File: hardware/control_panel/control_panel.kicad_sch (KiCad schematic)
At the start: 15 parts, among them J1 display, J13 motion and brightness sensors, J2 Conn_02x02_Odd_Even, J3 40HAT, J6 Conn_01x02, U3 TXB0108DQSR, U8 BCT0102

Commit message: hw layout
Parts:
- J3: footprint Connector_PinSocket_2.54mm:PinSocket_2x20_P2.54mm_Vertical -> project_footprints:raspberry_pi
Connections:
- net MOT: now also J13.2 (Pin_2), J3.7 (BCM4); no longer J13.4 (Pin_4)
- net RF.CE: now also U3.8 (A6); no longer U3.7 (A5)
- net RF.IRQ: now also U3.7 (A5); no longer U3.8 (A6)
- net SCL: now also J13.3 (Pin_3); no longer J13.2 (Pin_2)
- net SDA: now also J13.4 (Pin_4); no longer J13.3 (Pin_3)
- net UC.CE: now also U3.13 (B6); no longer U3.14 (B5)
- net UC.IRQ: now also U3.14 (B5); no longer U3.13 (B6)
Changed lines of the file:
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@@
     (stroke (width 0) (type default))
   )
-  (bus_entry (at 77.47 204.47) (size -2.54 2.54)
+  (bus_entry (at 77.47 201.93) (size -2.54 2.54)
     (stroke (width 0) (type default))
   )
@@
     (stroke (width 0) (type default))
   )
-  (bus_entry (at 77.47 201.93) (size -2.54 2.54)
+  (bus_entry (at 77.47 199.39) (size -2.54 2.54)
     (stroke (width 0) (type default))
   )
@@
     (stroke (width 0) (type default))
   )
-  (wire (pts (xy 74.93 204.47) (xy 68.58 204.47))
+  (wire (pts (xy 74.93 201.93) (xy 68.58 201.93))
     (stroke (width 0) (type default))
   )
@@
     (stroke (width 0) (type default))
   )
-  (bus (pts (xy 80.01 201.93) (xy 77.47 201.93))
+  (bus (pts (xy 80.01 199.39) (xy 77.47 199.39))
     (stroke (width 0) (type default))
   )
@@
     (stroke (width 0) (type default))
   )
-  (wire (pts (xy 68.58 201.93) (xy 71.12 201.93))
+  (wire (pts (xy 68.58 207.01) (xy 71.12 207.01))
     (stroke (width 0) (type default))
   )
@@
     (stroke (width 0) (type solid))
   )
-  (wire (pts (xy 74.93 207.01) (xy 68.58 207.01))
+  (wire (pts (xy 74.93 204.47) (xy 68.58 204.47))
     (stroke (width 0) (type default))
   )
@@
     (stroke (width 0) (type default))
   )
+  (wire (pts (xy 44.45 64.77) (xy 50.8 64.77))
+    (stroke (width 0) (type default))
+  )
   (wire (pts (xy 43.18 74.93) (xy 50.8 74.93))
     (stroke (width 0) (type default))
@@
     (stroke (width 0) (type default))
   )
-  (bus (pts (xy 77.47 201.93) (xy 77.47 204.47))
+  (bus (pts (xy 77.47 199.39) (xy 77.47 201.93))
     (stroke (width 0) (type default))
   )
@@
     (effects (font (size 1.27 1.27)) (justify right bottom))
   )
-  (label "RF.CE" (at 137.16 121.92 180) (fields_autoplaced)
+  (label "RF.CE" (at 137.16 124.46 180) (fields_autoplaced)
     (effects (font (size 1.27 1.27)) (justify right bottom))
   )
@@
     (effects (font (size 1.27 1.27)) (justify left bottom))
   )
-  (label "UC.IRQ" (at 157.48 124.46 0) (fields_autoplaced)
+  (label "UC.IRQ" (at 157.48 121.92 0) (fields_autoplaced)
     (effects (font (size 1.27 1.27)) (justify left bottom))
   )
@@
     (effects (font (size 1.27 1.27)) (justify left bottom))
   )
-  (label "MOT" (at 71.12 201.93 0) (fields_autoplaced)
+  (label "MOT" (at 71.12 207.01 0) (fields_autoplaced)
     (effects (font (size 1.27 1.27)) (justify left bottom))
   )
@@
     (effects (font (size 1.27 1.27)) (justify right bottom))
   )
-  (label "SDA" (at 71.12 204.47 0) (fields_autoplaced)
+  (label "SDA" (at 71.12 201.93 0) (fields_autoplaced)
     (effects (font (size 1.27 1.27)) (justify left bottom))
   )
@@
     (effects (font (size 1.27 1.27)) (justify left bottom))
   )
-  (label "SCL" (at 71.12 207.01 0) (fields_autoplaced)
+  (label "SCL" (at 71.12 204.47 0) (fields_autoplaced)
     (effects (font (size 1.27 1.27)) (justify left bottom))
   )
@@
     (effects (font (size 1.27 1.27)) (justify left bottom))
   )
-  (label "UC.CE" (at 157.48 121.92 0) (fields_autoplaced)
-    (effects (font (size 1.27 1.27)) (justify left bottom))
-  )
-  (label "RF.IRQ" (at 137.16 124.46 180) (fields_autoplaced)
+  (label "UC.CE" (at 157.48 124.46 0) (fields_autoplaced)
+    (effects (font (size 1.27 1.27)) (justify left bottom))
+  )
+  (label "RF.IRQ" (at 137.16 121.92 180) (fields_autoplaced)
     (effects (font (size 1.27 1.27)) (justify right bottom))
   )
@@
     (effects (font (size 1.27 1.27)) (justify right bottom))
   )
-  (label "{I2C}" (at 80.01 201.93 0) (fields_autoplaced)
+  (label "{I2C}" (at 80.01 199.39 0) (fields_autoplaced)
     (effects (font (size 1.27 1.27)) (justify left bottom))
   )
@@
     (effects (font (size 1.27 1.27)) (justify left bottom))
   )
-  (label "MOT" (at 39.37 82.55 180) (fields_autoplaced)
+  (label "MOT" (at 44.45 64.77 180) (fields_autoplaced)
     (effects (font (size 1.27 1.27)) (justify right bottom))
   )
@@
       (effects (font (size 1.27 1.27)))
     )
-    (property "Footprint" "Connector_PinSocket_2.54mm:PinSocket_2x20_P2.54mm_Vertical" (at 66.04 52.07 0)
+    (property "Footprint" "project_footprints:raspberry_pi" (at 66.04 52.07 0)
       (effects (font (size 1.27 1.27)) hide)
     )
@@
   )
   (symbol (lib_id "Connector_Generic:Conn_01x05") (at 63.5 204.47 180) (unit 1)
-    (in_bom yes) (on_board yes) (dnp no) (fields_autoplaced)
+    (in_bom yes) (on_board yes) (dnp no)
     (property "Reference" "J13" (at 63.5 194.4202 0)
       (effects (font (size 1.27 1.27)))
     )
-    (property "Value" "motion and brightness sensors" (at 63.5 196.9571 0)
-      (effects (font (size 1.27 1.27)))
-    )
+    (property "Value" "motion and brightness sensors" (at 54.61 196.9571 0)
+      (effects (font (size 1.27 1.27)))
+    )

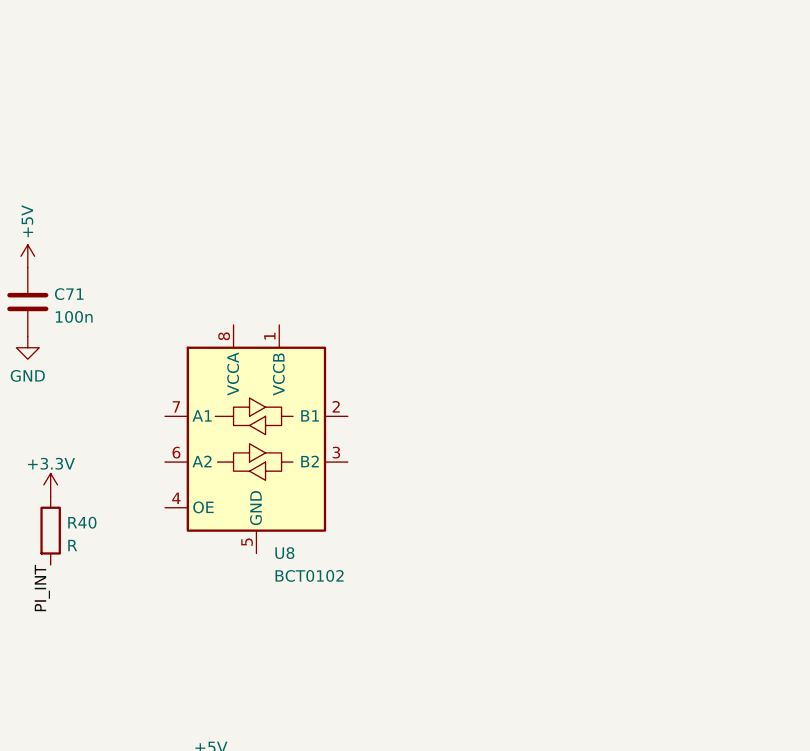
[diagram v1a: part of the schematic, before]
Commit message: led balance and corridor ready
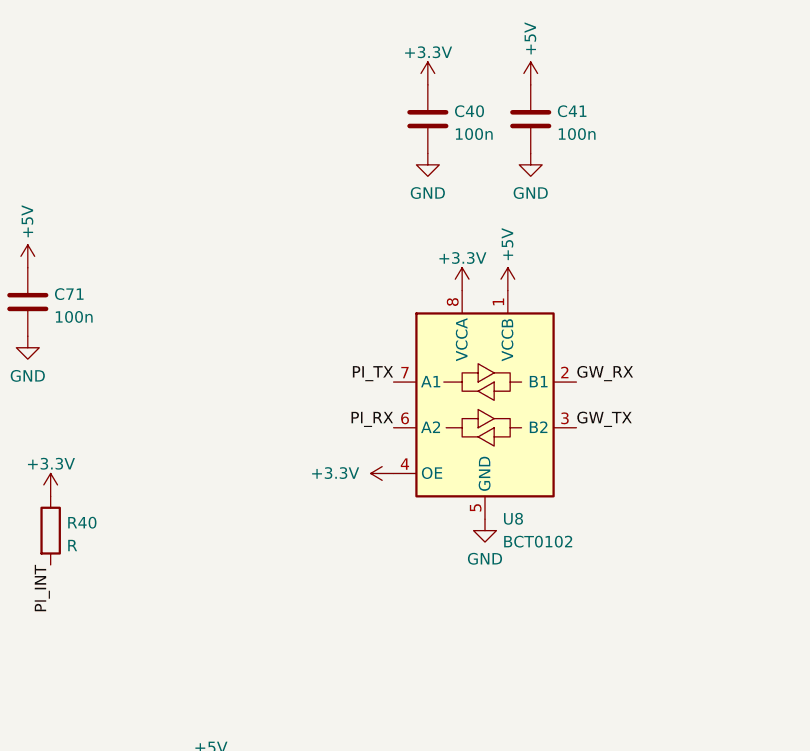
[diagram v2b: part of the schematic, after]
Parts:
- added C40, C41: 100n, Capacitor_SMD:C_0603_1608Metric, symbol Device:C
- J13: I2C address (none) -> 0x60
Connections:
- net +3.3V: now also U8.4 (OE), U8.8 (VCCA), C40.2
- net +5V: now also U8.1 (VCCB), C41.2
- net GND: now also U8.5 (GND), C40.1, C41.1
- net GW_RX: now also U8.2 (B1)
- net GW_TX: now also U8.3 (B2)
- net PI_RX: now also U8.6 (A2)
- net PI_TX: now also U8.7 (A1)
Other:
- moved on the sheet: U8
